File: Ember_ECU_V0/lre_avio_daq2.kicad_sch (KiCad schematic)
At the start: 150 parts, among them J1 Conn_01x02_Socket, J11 USB_C_Receptacle_USB2.0_16P, J12 XT30PW-F, J13 XT30PW-F, J14 XT30PW-F, J15 XT30PW-F, J16 XT30PW-F, J17 SMPW-CC-K-M, J18 SMPW-CC-K-M, J19 SMPW-CC-K-M, J2 DB25_Socket_MountingHoles, J23 DA15_Socket_MountingHoles, J24 DB25_Socket_MountingHoles, J3 XT60PW-M, Q1 SISA96DN-T1-GE3, Q2 SISA96DN-T1-GE3, Q3 SISA96DN-T1-GE3, SW1 SW_SPDT, U1 AMS1117-5.0, U10 ADS8353QPWRQ1, U11 ADS8353QPWRQ1, U12 STM32F412VGTx, U13 HX711, U14 HX711, U15 WS2812B-2020, U16 WS2812B-2020, U17 WS2812B-2020, U2 HX711, U3 SN65HVD230, U4 HX711, U5 AMS1117-5.0, U6 ADS8353QPWRQ1, U7 MAX31856, U8 MAX31856, U9 MAX31856, Y1 Crystal_8Mhz

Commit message: half routed ECU
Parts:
- added C7, C73, C75, C76: 47 uF, Capacitor_SMD:C_0603_1608Metric, symbol Device:C
- added C74: C, Capacitor_SMD:C_0603_1608Metric, symbol Device:C
- added D4, D5: ESDCAN02-2BWY, SOT65P210X110-3N, symbol ESDCAN02-2BWY:ESDCAN02-2BWY
- added J4: Conn_01x02_Socket, Connector_JST:JST_EH_B2B-EH-A_1x02_P2.50mm_Vertical, symbol Connector:Conn_01x02_Socket
- added R37: R, Resistor_SMD:R_0603_1608Metric, symbol Device:R
- added R38, R39, R40: 10k, Resistor_SMD:R_0603_1608Metric, symbol Device:R
- C1, C10, C11, C12, C13, C14, C15, C16, C17, C18, C19, C2, C20, C21, C22, C23, C24, C25, C26, C27, C28, C29, C3, C30, C31, C32, C33, C34, C35, C36, C37, C38, C39, C4, C40, C41, C42, C43, C44, C45, C46, C47, C48, C49, C5, C50, C51, C52, C53, C54, C55, C56, C57, C58, C59, C6, C60, C61, C62, C63, C64, C65, C66, C67, C68, C69, C70, C71, C72, C8, C9: footprint Capacitor_SMD:C_0201_0603Metric -> Capacitor_SMD:C_0603_1608Metric
- R1, R10, R11, R12, R13, R14, R15, R16, R17, R18, R19, R20, R21, R22, R23, R24, R25, R26, R27, R28, R29, R3, R30, R31, R32, R33, R4, R5, R6, R7, R8, R9: footprint Resistor_SMD:R_0201_0603Metric -> Resistor_SMD:R_0603_1608Metric
- R2: value 120 -> R; footprint Resistor_SMD:R_0201_0603Metric -> Resistor_SMD:R_0603_1608Metric
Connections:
- net 3v3: now also R38.2, R39.2, R40.2
- net ADS1_CS: now also R40.1
- net ADS2_CS: now also R38.1
- net ADS3_CS: now also R39.1
- net GND: now also C7.2, C73.1, C74.2, C75.1, C76.2, D4.3 (A_3), D5.3 (A_3)
- net pt1: now also R1.1; no longer R7.1
- net pt2: now also R9.1; no longer R10.1
- net pt3: now also R7.1; no longer R8.1
- net pt4: now also R10.1; no longer R17.1
- net pt5: now also R8.1; no longer R1.1
- net pt6: now also R17.1; no longer R9.1
- net CAN_H: now reaches J1.1 (Pin_1), R2.1, U3.7 (CANH)
- net CAN_H: now also C73.2, C75.2, D4.2 (A_2), D5.2 (A_2), J4.1 (Pin_1)
- net CAN_L: now reaches J1.2 (Pin_2), U3.6 (CANL)
- net CAN_L: now also C7.1, C76.1, D4.1 (A_1), D5.1 (A_1), J4.2 (Pin_2), R37.2; no longer R2.2
- new net: C74.1, R2.2, R37.1
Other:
- moved on the sheet: J1

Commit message: commit
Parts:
- R2: footprint Resistor_SMD:R_0603_1608Metric -> Resistor_SMD:R_0603_1608Metric_Pad0.98x0.95mm_HandSolder
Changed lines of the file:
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@@
 			)
 		)
-		(property "Footprint" "Resistor_SMD:R_0603_1608Metric"
+		(property "Footprint" "Resistor_SMD:R_0603_1608Metric_Pad0.98x0.95mm_HandSolder"
 			(at 497.332 166.37 90)
 			(hide yes)

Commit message: made changes to the pcb and fixed the schematic for can and add footptints
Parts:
- removed C75, C76: 47 uF, Capacitor_SMD:C_0603_1608Metric, symbol Device:C
- removed D5: ESDCAN02-2BWY, SOT65P210X110-3N, symbol ESDCAN02-2BWY:ESDCAN02-2BWY
- removed J4: Conn_01x02_Socket, Connector_JST:JST_EH_B2B-EH-A_1x02_P2.50mm_Vertical, symbol Connector:Conn_01x02_Socket
- removed U3: SN65HVD230, Package_SO:SOIC-8_3.9x4.9mm_P1.27mm, symbol Interface_CAN_LIN:SN65HVD230
- added C77, C78, C79, C80: 47pf, Capacitor_SMD:C_0603_1608Metric, symbol Device:C
- added C81: 100nF, Capacitor_SMD:C_0603_1608Metric, symbol Device:C_Small_US
- added J10, J20: Conn_01x02_Pin, Connector_JST:JST_EH_B2B-EH-A_1x02_P2.50mm_Vertical, symbol Connector:Conn_01x02_Pin
- added R41, R42, R43: 10K, Resistor_SMD:R_0603_1608Metric, symbol Device:R
- added U18: TCAN330, Package_SO:SOIC-8_3.9x4.9mm_P1.27mm, symbol Interface_CAN_LIN:TCAN330
- D1, D2: footprint RSX501LAM20TR:DIO_RB050LAM_ROM -> Diode_SMD:D_2114_3652Metric
- D4: footprint SOT65P210X110-3N -> ESDCAN02-2BWY:SOT65P210X110-3N
- J18, J19: footprint SMPWCCKM -> SMPW-CC-K-M:SMPWCCKM
- Q1, Q2, Q3: footprint SIS862DNT1GE3 -> footprints:MOSFET_1DN-T1-GE3_VIS
- U15, U16, U17: footprint SMT_12B-2020_WDS -> ggg:SMT_12B-2020_WDS
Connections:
- net SPI1_CS1 is gone; now on net TC1_CS: U7.9 (~{CS})
- net SPI1_CS2 is gone; now on net TC2_CS: U8.9 (~{CS})
- net SPI1_CS3 is gone; now on net TC3_CS: U9.9 (~{CS})
- net 3v3: now also C81.1, R41.1, R42.1, R43.1, U18.3 (VCC)
- net CAN_H: now also C78.2, C79.2, J10.2 (Pin_2), J20.2 (Pin_2), U18.7 (CANH)
- net CAN_L: now also C77.2, C80.2, J10.1 (Pin_1), J20.1 (Pin_1), U18.6 (CANL)
- net GND: now also C77.1, C78.1, C79.1, C80.1, C81.2, U18.2 (GND), U18.5 (SHDN), U18.8 (S)
- net TC1_CS: now also R43.2
- net TC2_CS: now also R41.2
- net TC3_CS: now also R42.2
- net CAN1_RX renamed CAN_RX
- net CAN_RX: now also U18.4 (RXD)
- net CAN1_TX renamed CAN_TX
- net CAN_TX: now also U18.1 (TXD)
- no-connect marks 69 -> 68
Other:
- note added: "CAN 1"
- note removed: "CAN"

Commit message: partial schematics fixes
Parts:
- added C? (x2): 47 uF, Capacitor_SMD:C_0603_1608Metric, symbol Device:C
- added D?: ESDCAN02-2BWY, ESDCAN02-2BWY:SOT65P210X110-3N, symbol ESDCAN02-2BWY:ESDCAN02-2BWY
- added J?: Conn_01x02_Socket, Connector_JST:JST_EH_B2B-EH-A_1x02_P2.50mm_Vertical, symbol Connector:Conn_01x02_Socket
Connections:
- net 7v4: no longer J12.1, J13.2, J14.1, J14.2, J15.1, J15.2, J16.1, J16.2, Q1.10 (D_6), Q1.7 (D_3), Q1.8 (D_4), Q1.9 (D_5), Q2.10 (D_6), Q2.7 (D_3), Q2.8 (D_4), Q2.9 (D_5), Q3.10 (D_6), Q3.7 (D_3), Q3.8 (D_4), Q3.9 (D_5), R20.1, R5.2
- net CAN_H: now also C?.2, D?.2 (A_2), J?.1 (Pin_1)
- net CAN_L: now also C?.1, D?.1 (A_1), J?.2 (Pin_2)
- net CAN_RX: now also U12.81 (PD0); no longer U12.70 (PA11)
- net CAN_TX: now also U12.82 (PD1); no longer U12.71 (PA12)
- net Conn1: no longer U12.81 (PD0)
- net Conn2: no longer U12.82 (PD1)
- net GND: now also C?.1, C?.2, D?.3 (A_3)
- net SPI2_MISO: now also U12.17 (PC2); no longer U12.53 (PB14)
- net SPI2_MOSI: now also U12.18 (PC3); no longer U12.54 (PB15)
- net SPI4_MISO: now also U12.4 (PE5); no longer U12.5 (PE6)
- net SPI4_MOSI: now also U12.5 (PE6); no longer U12.38 (PE7)
- net at Q1.11 (D_7), Q1.6 (D_2): now also Q1.5 (D_1)
- net ADS1_CS renamed SPI2_CS
- net ADS2_CS renamed SPI3_CS
- net ADS3_CS renamed SPI4_CS
- new net: J13.2, J14.1, J15.1, J16.1, R20.1
- new net: J15.2, Q3.10 (D_6), Q3.7 (D_3), Q3.8 (D_4), Q3.9 (D_5)
- new net: J14.2, Q2.10 (D_6), Q2.7 (D_3), Q2.8 (D_4), Q2.9 (D_5)
- new net: J16.2, Q1.10 (D_6), Q1.7 (D_3), Q1.8 (D_4), Q1.9 (D_5)
- new net 7v4_DOUT: J12.1, R5.2
- new net SDIO_CK: U12.54 (PB15)
- no-connect marks 68 -> 65

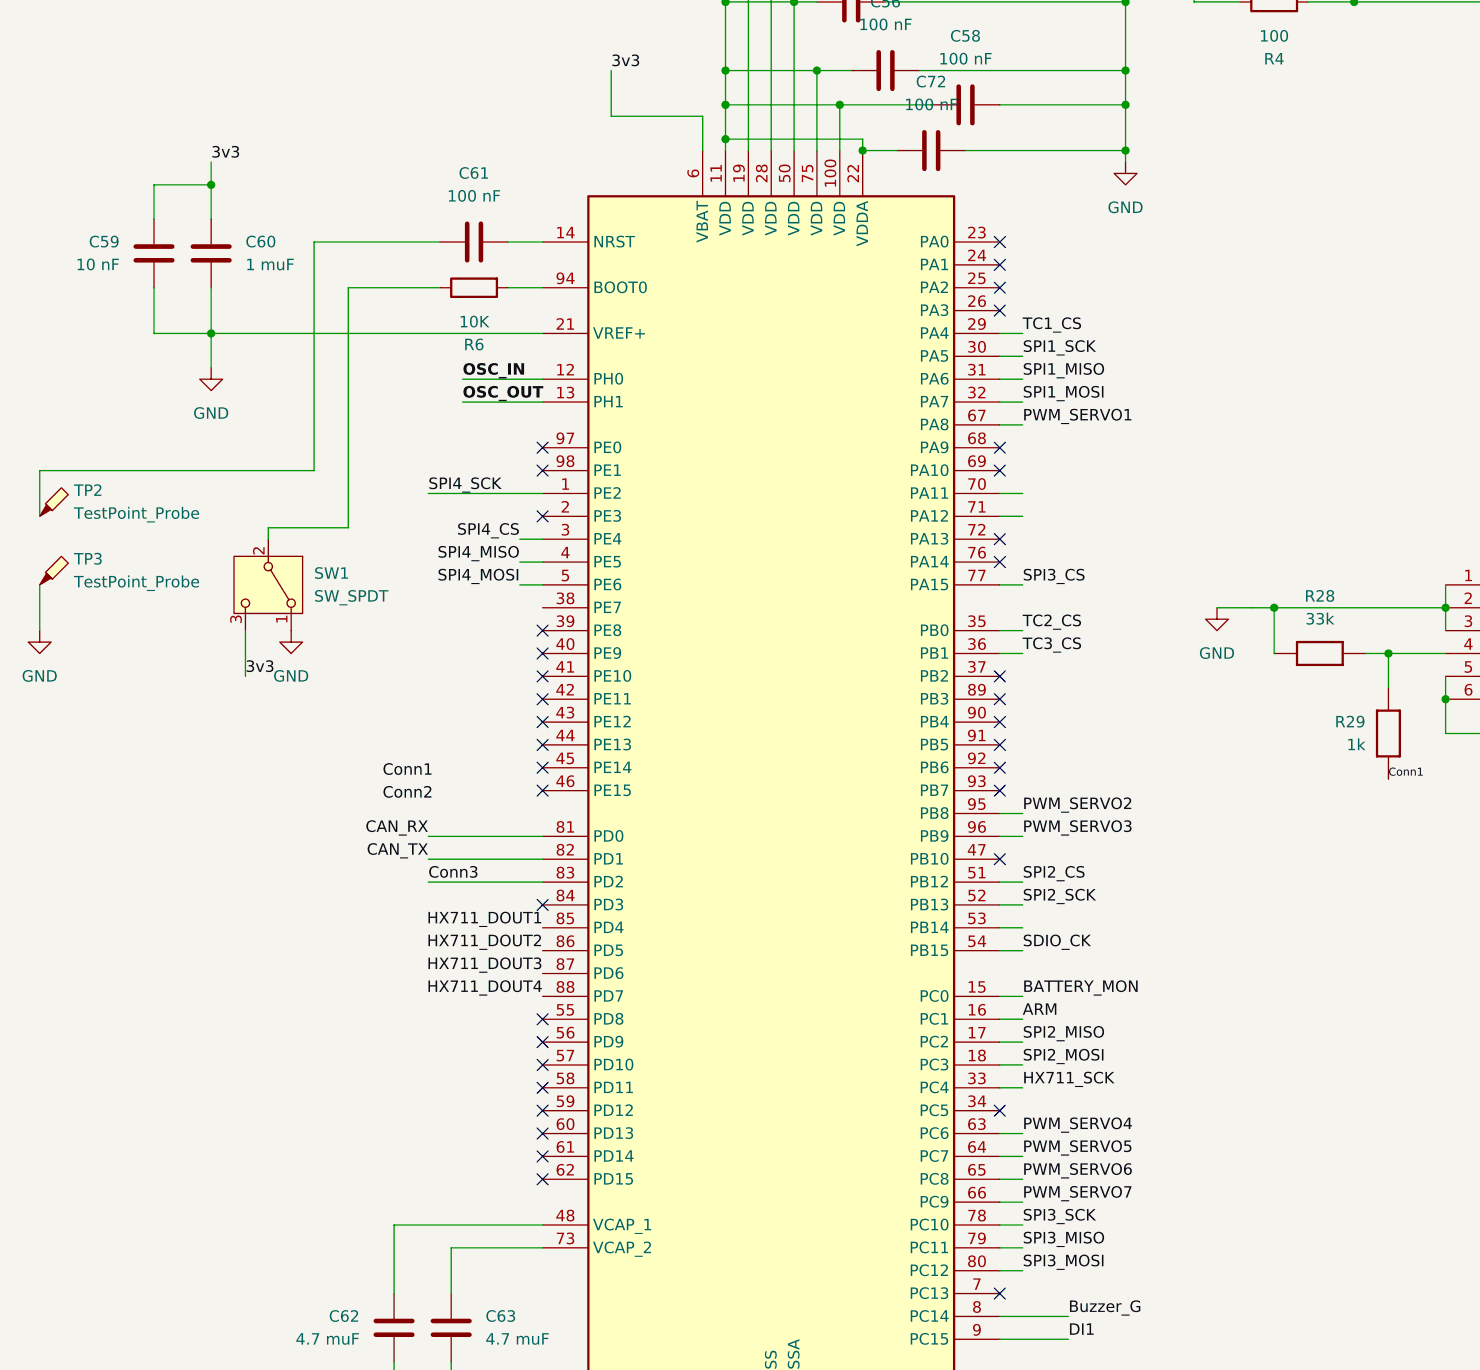
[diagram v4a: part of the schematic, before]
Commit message: changed pin layout and made compatible with mx file
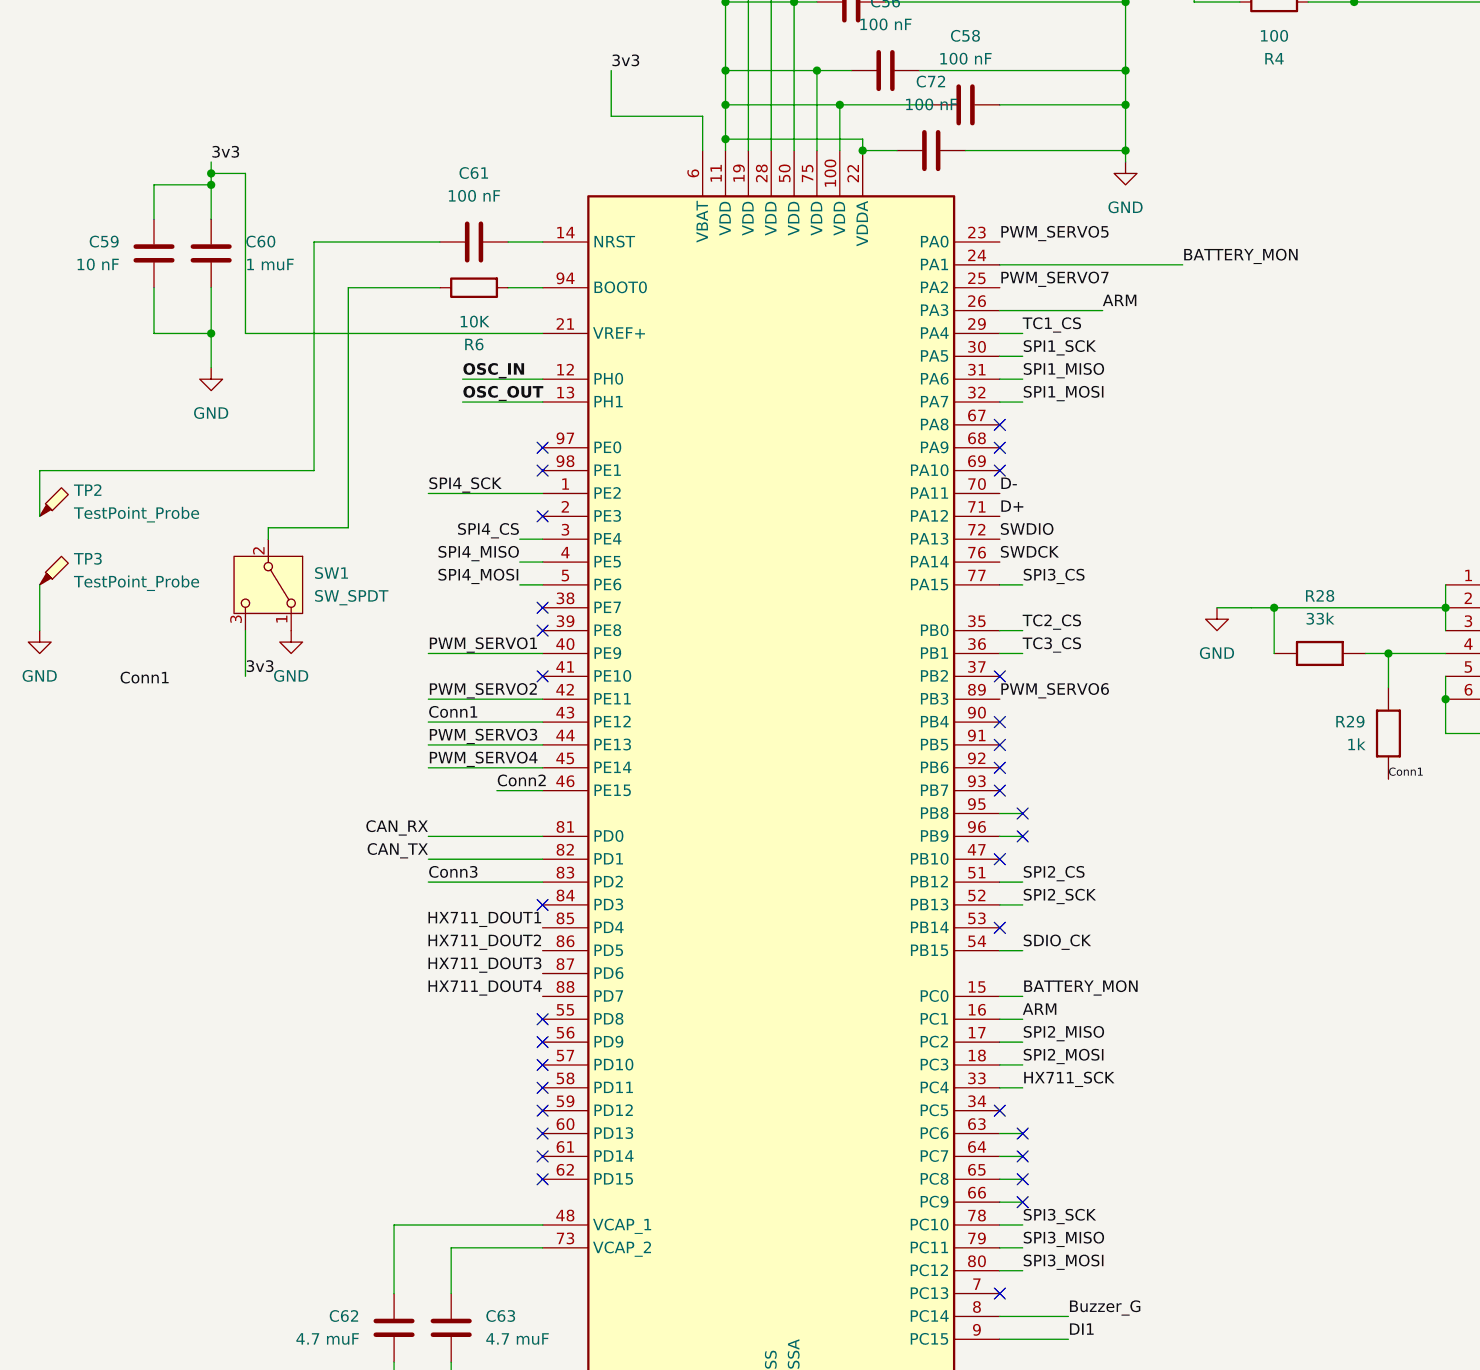
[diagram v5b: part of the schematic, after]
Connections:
- net 3v3: now also U12.21 (VREF+)
- net ARM: now also U12.26 (PA3)
- net BATTERY_MON: now also U12.24 (PA1)
- net Conn1: now also U12.43 (PE12)
- net Conn2: now also U12.46 (PE15)
- net D+: now also U12.71 (PA12)
- net D-: now also U12.70 (PA11)
- net GND: no longer U12.21 (VREF+)
- net PWM_SERVO1: now also U12.40 (PE9); no longer U12.67 (PA8)
- net PWM_SERVO2: now also U12.42 (PE11); no longer U12.95 (PB8)
- net PWM_SERVO3: now also U12.44 (PE13); no longer U12.96 (PB9)
- net PWM_SERVO4: now also U12.45 (PE14); no longer U12.63 (PC6)
- net PWM_SERVO5: now also U12.23 (PA0); no longer U12.64 (PC7)
- net PWM_SERVO6: now also U12.89 (PB3); no longer U12.65 (PC8)
- net PWM_SERVO7: now also U12.25 (PA2); no longer U12.66 (PC9)
- net SWDIO: now reaches U12.72 (PA13)
- net SWDCK: now reaches U12.76 (PA14)
- no-connect marks 65 -> 61

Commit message: mera last commit till 31/10
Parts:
- gave numbers to parts that had none: 4
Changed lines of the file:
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@@
 		(dnp no)
 		(fields_autoplaced yes)
-		(property "Reference" "D?"
+		(property "Reference" "D5"
 			(at 552.45 236.22 0)
 			(show_name no)
@@
 			(project "lre_avio_daq2"
 				(path "/436fb53c-203e-4b5d-ad3f-3d57776654d6"
-					(reference "D?")
+					(reference "D5")
 					(unit 1)
 				)
@@
 		(dnp no)
 		(fields_autoplaced yes)
-		(property "Reference" "J?"
+		(property "Reference" "J4"
 			(at 557.53 200.6599 0)
 			(show_name no)
@@
 			(project "lre_avio_daq2"
 				(path "/436fb53c-203e-4b5d-ad3f-3d57776654d6"
-					(reference "J?")
+					(reference "J4")
 					(unit 1)
 				)
@@
 		(dnp no)
 		(fields_autoplaced yes)
-		(property "Reference" "C?"
+		(property "Reference" "C76"
 			(at 551.18 208.2799 0)
 			(show_name no)
@@
 			(project "lre_avio_daq2"
 				(path "/436fb53c-203e-4b5d-ad3f-3d57776654d6"
-					(reference "C?")
+					(reference "C76")
 					(unit 1)
 				)
@@
 		(dnp no)
 		(fields_autoplaced yes)
-		(property "Reference" "C?"
+		(property "Reference" "C75"
 			(at 551.18 193.0399 0)
 			(show_name no)
@@
 			(project "lre_avio_daq2"
 				(path "/436fb53c-203e-4b5d-ad3f-3d57776654d6"
-					(reference "C?")
+					(reference "C75")
 					(unit 1)
 				)
